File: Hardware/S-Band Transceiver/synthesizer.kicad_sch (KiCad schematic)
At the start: 55 parts, among them J1 SMA, J2 SMA, U1 ADF4351, X1 XO32

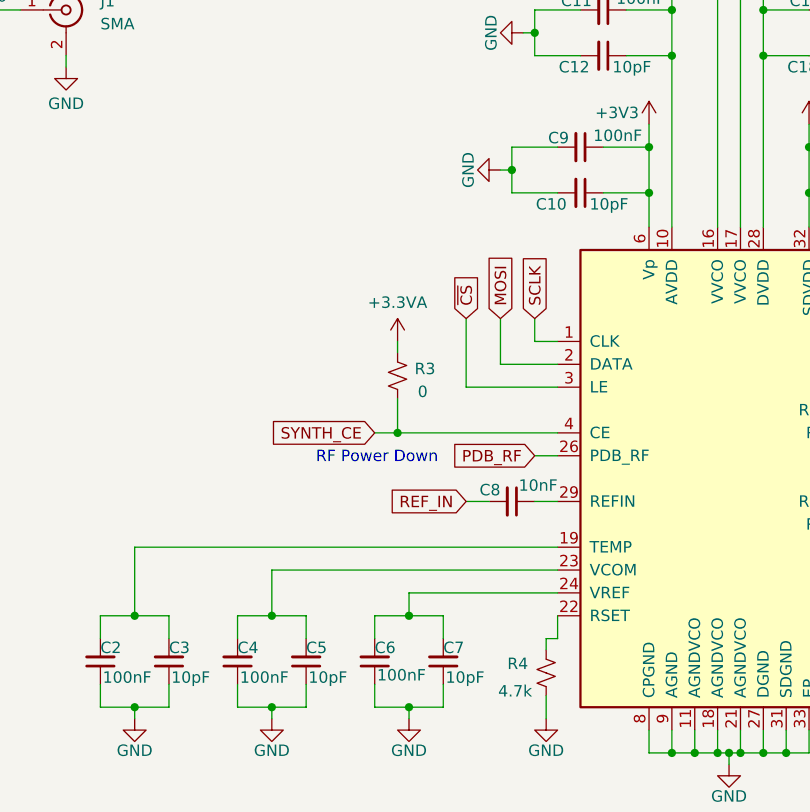
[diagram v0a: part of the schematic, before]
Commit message: Finished assigning footprints and starting board layout
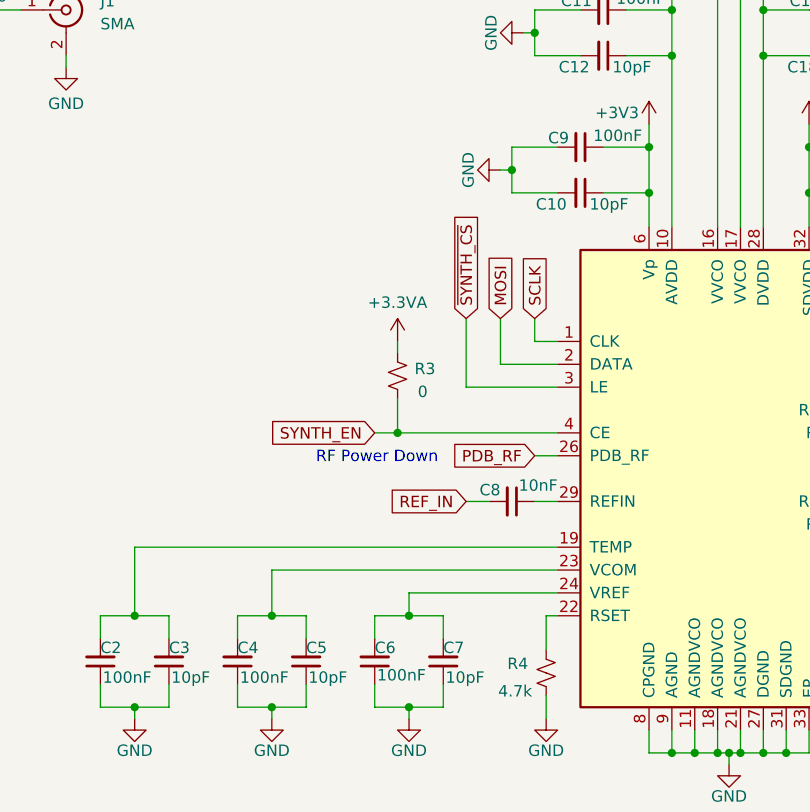
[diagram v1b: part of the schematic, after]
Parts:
- C1, C10, C11, C12, C13, C14, C15, C16, C17, C18, C19, C2, C20, C24, C25, C26, C27, C28, C29, C3, C30, C31, C32, C33, C4, C5, C6, C7, C8, C9: footprint (none) -> Capacitor_SMD:C_0402_1005Metric
- C21, C22, C23: footprint (none) -> Capacitor_SMD:C_0603_1608Metric
- D1: footprint (none) -> LED_SMD:LED_0805_2012Metric
- J1, J2: footprint (none) -> Connector_Coaxial:SMA_Samtec_SMA-J-P-X-ST-EM1_EdgeMount
- L1, L2, L3, L4, L5, L6, L7, L8: footprint (none) -> Inductor_SMD:L_0402_1005Metric
- R1, R2, R3, R4, R5, R6, R7, R8, R9: footprint (none) -> Resistor_SMD:R_0603_1608Metric
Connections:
- net SYNTH_CE renamed SYNTH_EN
- net ~{CS} renamed ~{SYNTH_CS}
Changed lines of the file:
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@@
 	(wire
 		(pts
+			(xy 123.19 116.84) (xy 124.46 116.84)
+		)
+		(stroke
+			(width 0)
+			(type default)
+		)
+	)
+	(wire
+		(pts
 			(xy 92.71 116.84) (xy 96.52 116.84)
 		)
@@
 	(wire
 		(pts
-			(xy 124.46 119.38) (xy 123.19 119.38)
-		)
-		(stroke
-			(width 0)
-			(type default)
-		)
-	)
-	(wire
-		(pts
 			(xy 144.78 132.08) (xy 147.32 132.08)
 		)
@@
 	(wire
 		(pts
-			(xy 123.19 119.38) (xy 123.19 120.65)
+			(xy 123.19 116.84) (xy 123.19 120.65)
 		)
 		(stroke
@@
 	(wire
 		(pts
-			(xy 124.46 119.38) (xy 124.46 116.84)
-		)
-		(stroke
-			(width 0)
-			(type default)
-		)
-	)
-	(wire
-		(pts
 			(xy 121.92 104.14) (xy 124.46 104.14)
 		)
@@
 		)
 	)
-	(global_label "~{CS}"
+	(global_label "~{SYNTH_CS}"
 		(shape input)
 		(at 114.3 83.82 90)
@@
 		)
 		(property "Intersheetrefs" "${INTERSHEET_REFS}"
-			(at 114.3 78.3553 90)
+			(at 114.3 71.461 90)
 			(effects
 				(font
@@
 		)
 	)
-	(global_label "SYNTH_CE"
+	(global_label "SYNTH_EN"
 		(shape input)
 		(at 104.14 96.52 180)
@@
 		)
 		(property "Intersheetrefs" "${INTERSHEET_REFS}"
-			(at 91.8415 96.52 0)
+			(at 91.781 96.52 0)
 			(effects
 				(font
@@
 			)
 		)
-		(property "Footprint" ""
+		(property "Footprint" "Capacitor_SMD:C_0402_1005Metric"
 			(at 231.14 113.03 0)
 			(effects
@@
 			)
 		)
-		(property "Footprint" ""
+		(property "Footprint" "Capacitor_SMD:C_0603_1608Metric"
 			(at 173.99 121.92 0)
 			(effects
@@
 			)
 		)
-		(property "Footprint" ""
+		(property "Footprint" "Capacitor_SMD:C_0402_1005Metric"
 			(at 129.54 54.61 0)
 			(effects
@@
 			)
 		)
-		(property "Footprint" ""
+		(property "Footprint" "Capacitor_SMD:C_0402_1005Metric"
 			(at 222.25 68.58 0)
 			(effects
@@
 			)
 		)
-		(property "Footprint" ""
+		(property "Footprint" "Capacitor_SMD:C_0402_1005Metric"
 			(at 96.52 121.92 0)
 			(effects
@@
 			)
 		)
-		(property "Footprint" ""
+		(property "Footprint" "Inductor_SMD:L_0402_1005Metric"
 			(at 215.9 66.04 0)
 			(effects
@@
 			)
 		)
-		(property "Footprint" ""
+		(property "Footprint" "Capacitor_SMD:C_0603_1608Metric"
 			(at 180.34 121.92 0)
 			(effects
@@
 			)
 		)
-		(property "Footprint" ""
+		(property "Footprint" "Capacitor_SMD:C_0402_1005Metric"
 			(at 152.4 35.56 0)
 			(effects
@@
 			)
 		)
-		(property "Footprint" ""
+		(property "Footprint" "Capacitor_SMD:C_0603_1608Metric"
 			(at 190.5 121.92 0)
 			(effects
@@
 			)
 		)
-		(property "Footprint" ""
+		(property "Footprint" "Connector_Coaxial:SMA_Samtec_SMA-J-P-X-ST-EM1_EdgeMount"
 			(at 254 81.28 0)
 			(effects
@@
 			)
 		)
-		(property "Footprint" ""
+		(property "Footprint" "Capacitor_SMD:C_0402_1005Metric"
 			(at 134.62 35.56 0)
 			(effects
@@
 			)
 		)
-		(property "Footprint" ""
+		(property "Footprint" "Inductor_SMD:L_0402_1005Metric"
 			(at 242.57 63.5 0)
 			(effects
@@
 			)
 		)
-		(property "Footprint" ""
+		(property "Footprint" "Capacitor_SMD:C_0402_1005Metric"
 			(at 154.94 49.53 0)
 			(effects
@@
 			)
 		)
-		(property "Footprint" ""
+		(property "Footprint" "Capacitor_SMD:C_0402_1005Metric"
 			(at 231.14 63.5 0)
 			(effects
@@
 			)
 		)
-		(property "Footprint" ""
+		(property "Footprint" "Inductor_SMD:L_0402_1005Metric"
 			(at 242.57 130.81 0)
 			(effects
@@
 			)
 		)
-		(property "Footprint" ""
+		(property "Footprint" "Capacitor_SMD:C_0402_1005Metric"
 			(at 222.25 76.2 0)
 			(effects
@@
 			)
 		)
-		(property "Footprint" ""
+		(property "Footprint" "Capacitor_SMD:C_0402_1005Metric"
 			(at 111.76 121.92 0)
 			(effects
@@
 			)
 		)
-		(property "Footprint" ""
+		(property "Footprint" "Capacitor_SMD:C_0402_1005Metric"
 			(at 73.66 121.92 0)
 			(effects
@@
 			)
 		)
-		(property "Footprint" ""
+		(property "Footprint" "Capacitor_SMD:C_0402_1005Metric"
 			(at 231.14 81.28 0)
 			(effects
@@
 			)
 		)
-		(property "Footprint" ""
+		(property "Footprint" "Resistor_SMD:R_0603_1608Metric"
 			(at 168.91 134.62 0)
 			(effects
@@
 			)
 		)
-		(property "Footprint" ""
+		(property "Footprint" "Capacitor_SMD:C_0402_1005Metric"
 			(at 160.02 64.77 0)
 			(effects
@@
 			)
 		)
-		(property "Footprint" ""
+		(property "Footprint" "Capacitor_SMD:C_0402_1005Metric"
 			(at 154.94 54.61 0)
 			(effects
@@
 			)
 		)
-		(property "Footprint" ""
+		(property "Footprint" "Inductor_SMD:L_0402_1005Metric"
 			(at 215.9 115.57 0)
 			(effects
@@
 			)
 		)
-		(property "Footprint" ""
+		(property "Footprint" "Capacitor_SMD:C_0402_1005Metric"
 			(at 231.14 130.81 0)
 			(effects
@@
 			)
 		)
-		(property "Footprint" ""
+		(property "Footprint" "Resistor_SMD:R_0603_1608Metric"
 			(at 180.34 129.54 0)
 			(effects
@@
 			)
 		)
-		(property "Footprint" ""
+		(property "Footprint" "Capacitor_SMD:C_0402_1005Metric"
 			(at 34.29 31.75 0)
 			(effects
@@
 			)
 		)
-		(property "Footprint" ""
+		(property "Footprint" "Inductor_SMD:L_0402_1005Metric"
 			(at 242.57 113.03 0)
 			(effects
@@
 			)
 		)
-		(property "Footprint" ""
+		(property "Footprint" "Resistor_SMD:R_0603_1608Metric"
 			(at 180.34 138.43 0)
 			(effects
@@
 			)
 		)
-		(property "Footprint" ""
+		(property "Footprint" "LED_SMD:LED_0805_2012Metric"
 			(at 186.69 76.2 90)
 			(effects
@@
 			)
 		)
-		(property "Footprint" ""
+		(property "Footprint" "Capacitor_SMD:C_0402_1005Metric"
 			(at 88.9 121.92 0)
 			(effects
@@
 			)
 		)
-		(property "Footprint" ""
+		(property "Footprint" "Capacitor_SMD:C_0402_1005Metric"
 			(at 127 69.85 0)
 			(effects
@@
 			)
 		)
-		(property "Footprint" ""
+		(property "Footprint" "Capacitor_SMD:C_0402_1005Metric"
 			(at 129.54 49.53 0)
 			(effects
@@
 			)
 		)
-		(property "Footprint" ""
+		(property "Footprint" "Resistor_SMD:R_0603_1608Metric"
 			(at 185.42 116.84 0)
 			(effects
@@
 			)
 		)
-		(property "Footprint" ""
+		(property "Footprint" "Resistor_SMD:R_0603_1608Metric"
 			(at 106.68 90.17 0)
 			(effects
@@
 			)
 		)
-		(property "Footprint" ""
+		(property "Footprint" "Capacitor_SMD:C_0402_1005Metric"
 			(at 222.25 72.39 0)
 			(effects
@@
 			)
 		)
-		(property "Footprint" ""
+		(property "Footprint" "Inductor_SMD:L_0402_1005Metric"
 			(at 215.9 128.27 0)
 			(effects
@@
 			)
 		)
-		(property "Footprint" ""
+		(property "Footprint" "Resistor_SMD:R_0603_1608Metric"
 			(at 186.69 69.85 0)
 			(effects
@@
 			)
 		)
-		(property "Footprint" ""
+		(property "Footprint" "Capacitor_SMD:C_0402_1005Metric"
 			(at 222.25 118.11 0)
 			(effects
@@
 			)
 		)
-		(property "Footprint" ""
+		(property "Footprint" "Capacitor_SMD:C_0402_1005Metric"
 			(at 127 64.77 0)
 			(effects
@@
 			)
 		)
-		(property "Footprint" ""
+		(property "Footprint" "Inductor_SMD:L_0402_1005Metric"
 			(at 242.57 81.28 0)
 			(effects
@@
 			)
 		)
-		(property "Footprint" ""
+		(property "Footprint" "Capacitor_SMD:C_0402_1005Metric"
 			(at 160.02 69.85 0)
 			(effects
@@
 			)
 		)
-		(property "Footprint" ""
+		(property "Footprint" "Resistor_SMD:R_0603_1608Metric"
 			(at 55.88 40.64 0)
 			(effects
@@
 			)
 		)
-		(property "Footprint" ""
+		(property "Footprint" "Inductor_SMD:L_0402_1005Metric"
 			(at 215.9 78.74 0)
 			(effects
@@
 			)
 		)
-		(property "Footprint" ""
+		(property "Footprint" "Resistor_SMD:R_0603_1608Metric"
 			(at 60.96 45.72 0)
 			(effects
@@
 			)
 		)
-		(property "Footprint" ""
+		(property "Footprint" "Capacitor_SMD:C_0402_1005Metric"
 			(at 134.62 40.64 0)
 			(effects
@@
 			)
 		)
-		(property "Footprint" ""
+		(property "Footprint" "Capacitor_SMD:C_0402_1005Metric"
 			(at 222.25 121.92 0)
 			(effects
@@
 			)
 		)
-		(property "Footprint" ""
+		(property "Footprint" "Resistor_SMD:R_0603_1608Metric"
 			(at 123.19 123.19 0)
 			(effects
@@
 			)
 		)
-		(property "Footprint" ""
+		(property "Footprint" "Capacitor_SMD:C_0402_1005Metric"
 			(at 222.25 125.73 0)
 			(effects
@@
 			)
 		)
-		(property "Footprint" ""
+		(property "Footprint" "Capacitor_SMD:C_0402_1005Metric"
 			(at 104.14 121.92 0)
 			(effects
@@
 			)
 		)
-		(property "Footprint" ""
+		(property "Footprint" "Capacitor_SMD:C_0402_1005Metric"
 			(at 81.28 121.92 0)
 			(effects
@@
 			)
 		)
-		(property "Footprint" ""
+		(property "Footprint" "Capacitor_SMD:C_0402_1005Metric"
 			(at 152.4 40.64 0)
 			(effects
@@
 			)
 		)
-		(property "Footprint" ""
+		(property "Footprint" "Connector_Coaxial:SMA_Samtec_SMA-J-P-X-ST-EM1_EdgeMount"
 			(at 69.85 49.53 0)
 			(effects
@@
 			)
 		)
-		(property "Footprint" ""
+		(property "Footprint" "Capacitor_SMD:C_0402_1005Metric"
 			(at 119.38 104.14 0)
 			(effects

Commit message: Updating Capacitors and LEDs in schematic
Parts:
- D1: value LED_Small -> 150080VS75000
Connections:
- net +3V3 is gone; now on net +3.3VA: C10.1, C11.1, C12.1, C17.2, C18.2, C19.2, C20.2, C9.1, U1.10 (AVDD), U1.28 (DVDD), U1.32 (SDVDD), U1.6 (Vp)

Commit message: Updating synthesizer schematic and layout
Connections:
- net SYNTH_TX is gone; now on net LO+: L5.2
- net LO+: no longer L7.2
- net LO-: now also L6.2; no longer L8.2
- net at J2.1 (In): now also L7.2; no longer L6.2
- new net AUX_OUT: L8.2
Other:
- moved on the sheet: J2
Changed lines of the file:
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@@
 	)
 	(junction
+		(at 247.65 130.81)
+		(diameter 0)
+		(color 0 0 0 0)
+	)
+	(junction
 		(at 106.68 96.52)
 		(diameter 0)
@@
 	(wire
 		(pts
+			(xy 247.65 129.54) (xy 247.65 130.81)
+		)
+		(stroke
+			(width 0)
+			(type default)
+		)
+	)
+	(wire
+		(pts
 			(xy 147.32 129.54) (xy 147.32 132.08)
 		)
@@
 	(wire
 		(pts
-			(xy 254 86.36) (xy 254 88.9)
-		)
-		(stroke
-			(width 0)
-			(type default)
-		)
-	)
-	(wire
-		(pts
 			(xy 142.24 132.08) (xy 143.51 132.08)
 		)
@@
 	(wire
 		(pts
+			(xy 247.65 130.81) (xy 250.19 130.81)
+		)
+		(stroke
+			(width 0)
+			(type default)
+		)
+	)
+	(wire
+		(pts
 			(xy 123.19 116.84) (xy 123.19 120.65)
 		)
@@
 	(wire
 		(pts
-			(xy 245.11 130.81) (xy 250.19 130.81)
+			(xy 245.11 130.81) (xy 247.65 130.81)
 		)
 		(stroke
@@
 		)
 	)
+	(wire
+		(pts
+			(xy 255.27 118.11) (xy 255.27 119.38)
+		)
+		(stroke
+			(width 0)
+			(type default)
+		)
+	)
 	(text "Lock Detect"
 		(exclude_from_sim no)
@@
 	(text "0dBm"
 		(exclude_from_sim no)
-		(at 255.524 60.706 0)
+		(at 256.794 128.016 0)
 		(effects
 			(font
@@
 		)
 	)
+	(global_label "AUX_OUT"
+		(shape input)
+		(at 247.65 129.54 90)
+		(fields_autoplaced yes)
+		(effects
+			(font
+				(size 1.27 1.27)
+			)
+			(justify left)
+		)
+		(property "Intersheetrefs" "${INTERSHEET_REFS}"
+			(at 247.65 118.33 90)
+			(effects
+				(font
+					(size 1.27 1.27)
+				)
+				(justify left)
+				(hide yes)
+			)
+		)
+	)
 	(global_label "XO_EN"
 		(shape input)
@@
 	(global_label "LO-"
 		(shape input)
-		(at 250.19 130.81 0)
+		(at 248.92 81.28 0)
 		(fields_autoplaced yes)
 		(effects
@@
 		)
 		(property "Intersheetrefs" "${INTERSHEET_REFS}"
-			(at 257.1062 130.81 0)
+			(at 255.8362 81.28 0)
 			(effects
 				(font
@@
 	(global_label "SYNTH_TX"
 		(shape input)
-		(at 248.92 63.5 0)
+		(at 250.19 130.81 0)
 		(fields_autoplaced yes)
 		(effects
@@
 		)
 		(property "Intersheetrefs" "${INTERSHEET_REFS}"
-			(at 260.9766 63.5 0)
+			(at 262.2466 130.81 0)
 			(effects
 				(font
@@
 	(global_label "LO+"
 		(shape input)
-		(at 250.19 113.03 0)
+		(at 248.92 63.5 0)
 		(fields_autoplaced yes)
 		(effects
@@
 		)
 		(property "Intersheetrefs" "${INTERSHEET_REFS}"
-			(at 257.1062 113.03 0)
+			(at 255.8362 63.5 0)
 			(effects
 				(font
@@
 	(symbol
 		(lib_id "Connector:Conn_Coaxial")
-		(at 254 81.28 0)
+		(at 255.27 113.03 0)
 		(unit 1)
 		(exclude_from_sim no)
@@
 		(fields_autoplaced yes)
 		(property "Reference" "J2"
-			(at 257.81 80.3031 0)
+			(at 259.08 112.0531 0)
 			(effects
 				(font
@@
 		)
 		(property "Value" "SMA"
-			(at 257.81 82.8431 0)
+			(at 259.08 114.5931 0)
 			(effects
 				(font
@@
 		)
 		(property "Footprint" "Connector_Coaxial:SMA_Samtec_SMA-J-P-X-ST-EM1_EdgeMount"
-			(at 254 81.28 0)
+			(at 255.27 113.03 0)
 			(effects
 				(font
@@
 		)
 		(property "Datasheet" " ~"
-			(at 254 81.28 0)
+			(at 255.27 113.03 0)
 			(effects
 				(font
@@
 		)
 		(property "Description" "coaxial connector (BNC, SMA, SMB, SMC, Cinch/RCA, LEMO, ...)"
-			(at 254 81.28 0)
+			(at 255.27 113.03 0)
 			(effects
 				(font
@@
 	(symbol
 		(lib_id "power:GND")
-		(at 254 88.9 0)
+		(at 255.27 119.38 0)
 		(unit 1)
 		(exclude_from_sim no)
@@
 		(on_board yes)
 		(dnp no)
-		(fields_autoplaced yes)
 		(property "Reference" "#PWR030"
-			(at 254 95.25 0)
+			(at 255.27 125.73 0)
 			(effects
 				(font
@@
 		)
 		(property "Value" "GND"
-			(at 254 93.98 0)
+			(at 258.826 121.412 0)
 			(effects
 				(font
@@
 		)
 		(property "Footprint" ""
-			(at 254 88.9 0)
+			(at 255.27 119.38 0)
 			(effects
 				(font
@@
 		)
 		(property "Datasheet" ""
-			(at 254 88.9 0)
+			(at 255.27 119.38 0)
 			(effects
 				(font
@@
 		)
 		(property "Description" "Power symbol creates a global label with name \"GND\" , ground"
-			(at 254 88.9 0)
+			(at 255.27 119.38 0)
 			(effects
 				(font

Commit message: Updating board layout, adding inductor to LNA input
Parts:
- R3: value 0 -> 10k
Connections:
- net AUX_OUT renamed SYNTH_TX
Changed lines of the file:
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@@
 	)
 	(junction
-		(at 247.65 130.81)
-		(diameter 0)
-		(color 0 0 0 0)
-	)
-	(junction
 		(at 106.68 96.52)
 		(diameter 0)
@@
 	(wire
 		(pts
-			(xy 247.65 129.54) (xy 247.65 130.81)
-		)
-		(stroke
-			(width 0)
-			(type default)
-		)
-	)
-	(wire
-		(pts
 			(xy 147.32 129.54) (xy 147.32 132.08)
 		)
@@
 	(wire
 		(pts
-			(xy 247.65 130.81) (xy 250.19 130.81)
+			(xy 245.11 130.81) (xy 250.19 130.81)
 		)
 		(stroke
@@
 	(wire
 		(pts
-			(xy 245.11 130.81) (xy 247.65 130.81)
-		)
-		(stroke
-			(width 0)
-			(type default)
-		)
-	)
-	(wire
-		(pts
 			(xy 30.48 31.75) (xy 31.75 31.75)
 		)
@@
 		)
 	)
-	(global_label "AUX_OUT"
-		(shape input)
-		(at 247.65 129.54 90)
-		(fields_autoplaced yes)
-		(effects
-			(font
-				(size 1.27 1.27)
-			)
-			(justify left)
-		)
-		(property "Intersheetrefs" "${INTERSHEET_REFS}"
-			(at 247.65 118.33 90)
-			(effects
-				(font
-					(size 1.27 1.27)
-				)
-				(justify left)
-				(hide yes)
-			)
-		)
-	)
 	(global_label "XO_EN"
 		(shape input)
@@
 			)
 		)
-		(property "Value" "0"
+		(property "Value" "10k"
 			(at 109.474 91.948 0)
 			(effects
